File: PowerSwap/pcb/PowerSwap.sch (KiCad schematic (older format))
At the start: 11 parts

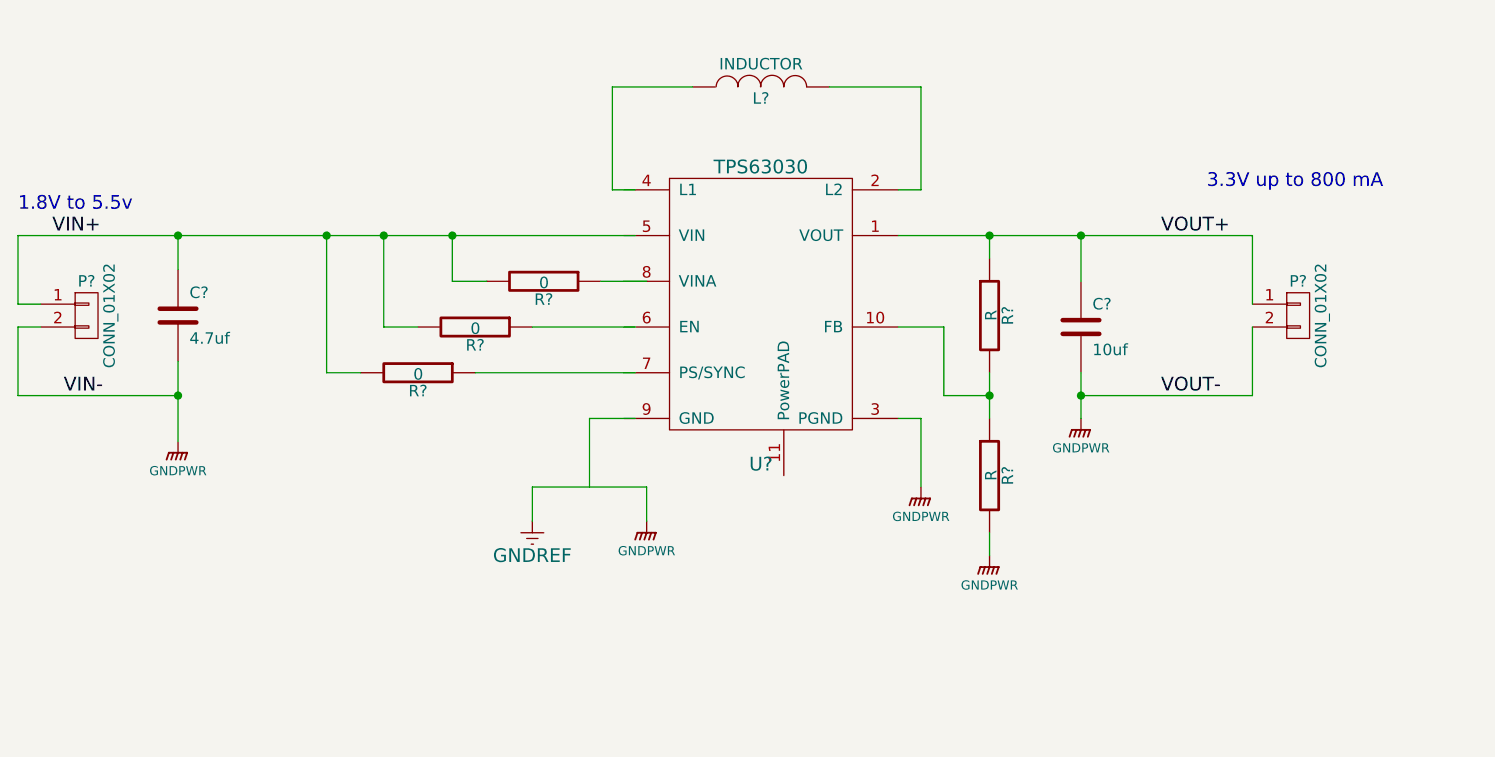
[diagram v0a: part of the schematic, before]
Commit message: PS updated schematic with testpoints and option a/b applications
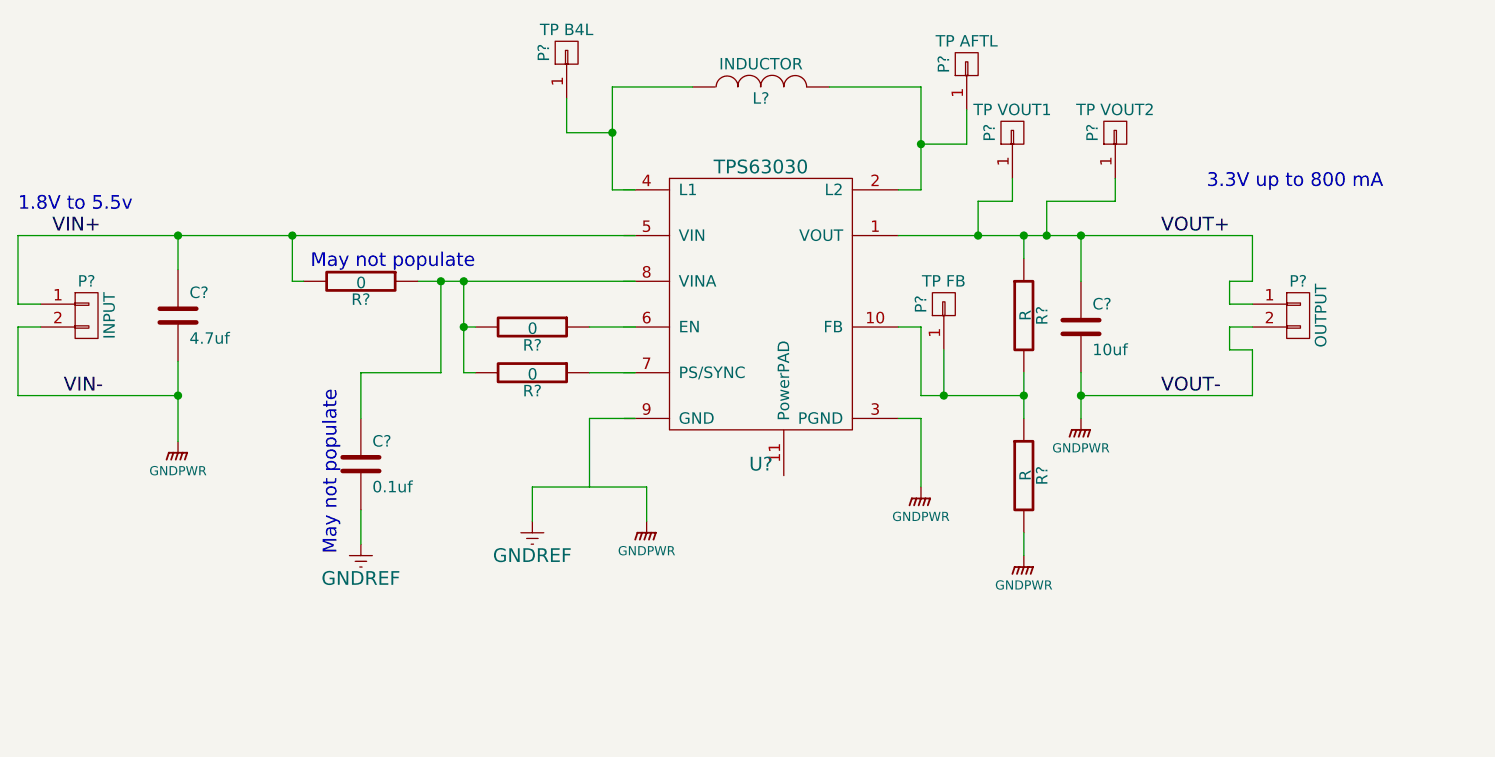
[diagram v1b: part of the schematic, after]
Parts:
- removed R? (x3): 0, symbol R
- added C?: 0.1uf, symbol C
- added P?: TP FB, symbol CONN_01X01
- added P?: TP B4L, symbol CONN_01X01
- added P?: TP AFTL, symbol CONN_01X01
- added P?: TP VOUT1, symbol CONN_01X01
- added P?: TP VOUT2, symbol CONN_01X01
- added R? (x3): 0, symbol R
- P?: value CONN_01X02 -> OUTPUT
- P?: value CONN_01X02 -> INPUT
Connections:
- wire segments 42 -> 62
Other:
- note added: "May not populate"
- moved on the sheet: R?

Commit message: PS updated schematic with testpoints and option a/b applications
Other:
- note removed: "3.3V up to 800 mA"
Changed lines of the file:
@@
 Wire Wire Line
 	4750 2850 6300 2850
-Text Notes 6100 2650 0    60   ~ 0
-3.3V up to 800 mA
 Wire Wire Line
 	5550 2850 5550 3050

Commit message: PS updated schematic with testpoints and option a/b applications
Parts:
- C?: value 4.7uf -> 4.7/10uf
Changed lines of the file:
@@
 P 1600 3200
 F 0 "C?" H 1650 3300 50  0000 L CNN
-F 1 "4.7uf" H 1650 3100 50  0000 L CNN
+F 1 "4.7/10uf" H 1650 3100 50  0000 L CNN
 F 2 "" H 1638 3050 30  0000 C CNN
 F 3 "" H 1600 3200 60  0000 C CNN

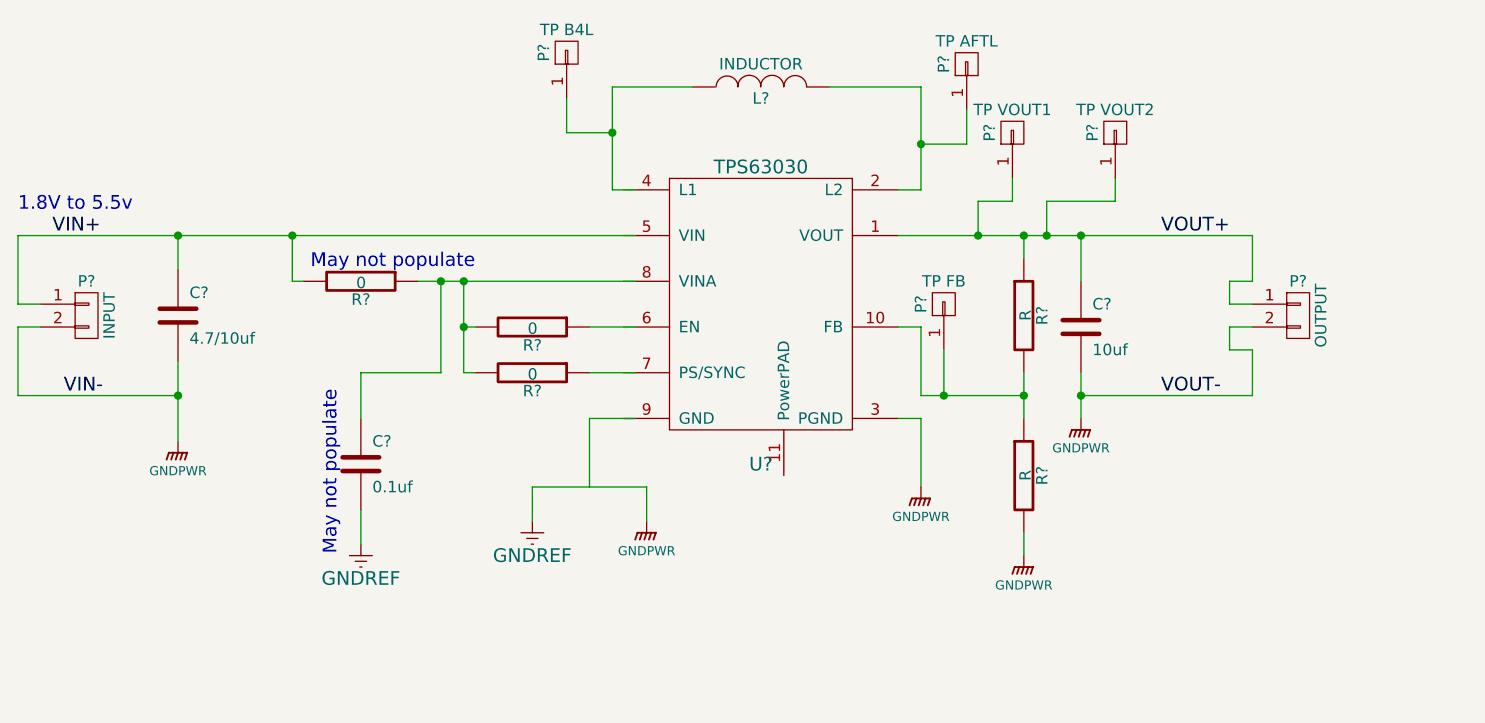
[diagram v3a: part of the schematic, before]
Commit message: PS added PowerPAD to tps6030, created footprint for tps6030
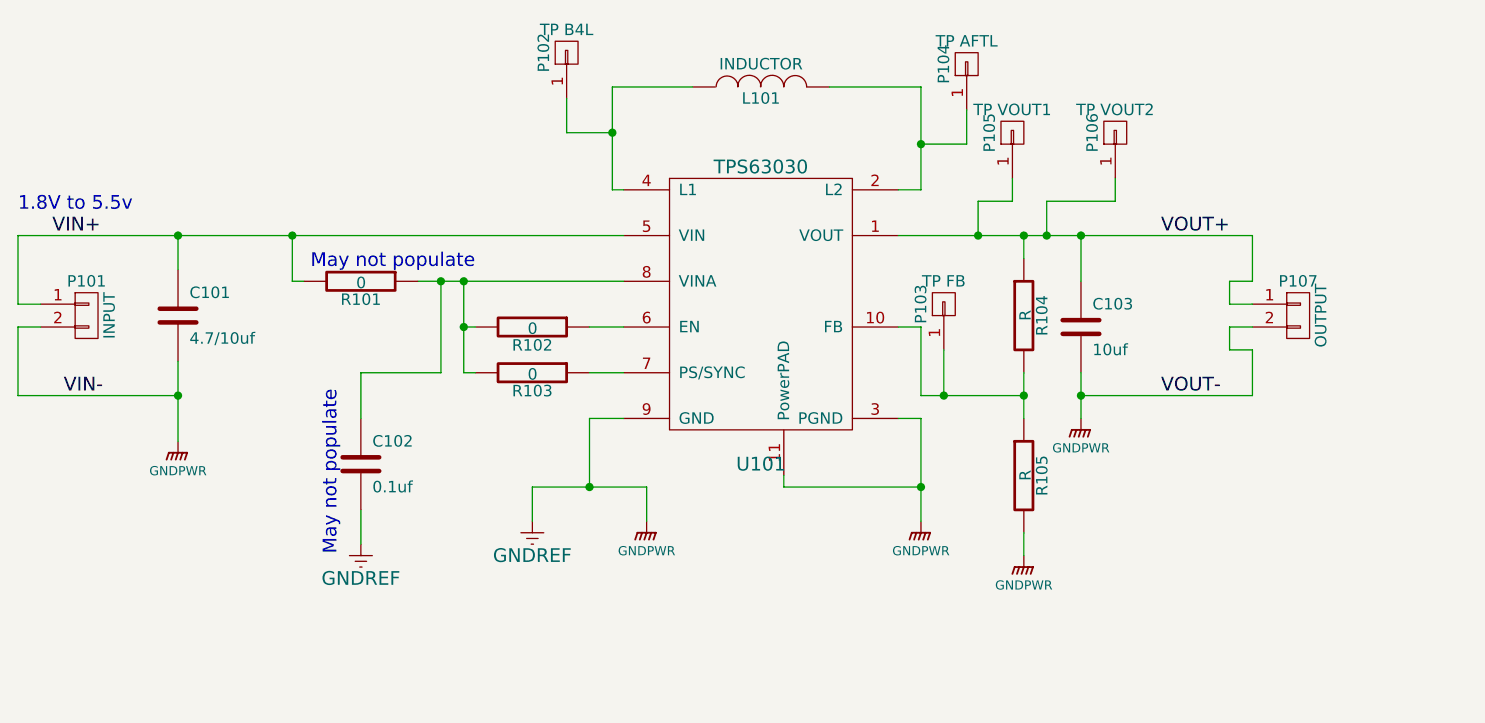
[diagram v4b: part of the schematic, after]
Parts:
- gave numbers to parts that had none: 17
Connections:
- wire segments 62 -> 64
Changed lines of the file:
@@
 v1
 $Comp
-L TPS63030 U?
+L TPS63030 U101
 U 1 1 55BC574B
 P 4150 3150
-F 0 "U?" H 4150 2450 60  0000 C CNN
+F 0 "U101" H 4150 2450 60  0000 C CNN
 F 1 "TPS63030" H 4150 3750 60  0000 C CNN
 F 2 "" H 4150 3150 60  0000 C CNN
@@
 $EndComp
 $Comp
-L INDUCTOR L?
+L INDUCTOR L101
 U 1 1 55BC57E7
 P 4150 2200
-F 0 "L?" V 4100 2200 50  0000 C CNN
+F 0 "L101" V 4100 2200 50  0000 C CNN
 F 1 "INDUCTOR" V 4250 2200 50  0000 C CNN
 F 2 "" H 4150 2200 60  0000 C CNN
@@
 $EndComp
 Wire Wire Line
-	3500 2650 3600 2650
-Wire Wire Line
-	3500 2200 3500 2650
-Wire Wire Line
 	3500 2200 3850 2200
 Wire Wire Line
@@
 Wire Wire Line
 	4850 2200 4450 2200
-Wire Wire Line
-	900  2850 3600 2850
 Text Notes 900  2750 0    60   ~ 0
 1.8V to 5.5v
@@
 Connection ~ 1600 2850
 $Comp
-L C C?
+L C C101
 U 1 1 55BC58C4
 P 1600 3200
-F 0 "C?" H 1650 3300 50  0000 L CNN
+F 0 "C101" H 1650 3300 50  0000 L CNN
 F 1 "4.7/10uf" H 1650 3100 50  0000 L CNN
 F 2 "" H 1638 3050 30  0000 C CNN
@@
 Connection ~ 1600 3550
 $Comp
-L GNDPWR #PWR?
+L GNDPWR #PWR01
 U 1 1 55BC592A
 P 1600 3750
-F 0 "#PWR?" H 1600 3550 40  0001 C CNN
+F 0 "#PWR01" H 1600 3550 40  0001 C CNN
 F 1 "GNDPWR" H 1600 3620 40  0000 C CNN
 F 2 "" H 1600 3700 60  0000 C CNN
@@
 $EndComp
 Wire Wire Line
-	3600 3650 3400 3650
-Wire Wire Line
-	3400 3650 3400 3950
-Wire Wire Line
 	3150 3950 3650 3950
 Wire Wire Line
@@
 	3650 3950 3650 4100
 $Comp
-L GNDPWR #PWR?
+L GNDPWR #PWR02
 U 1 1 55BC59FC
 P 3650 4100
-F 0 "#PWR?" H 3650 3900 40  0001 C CNN
+F 0 "#PWR02" H 3650 3900 40  0001 C CNN
 F 1 "GNDPWR" H 3650 3970 40  0000 C CNN
 F 2 "" H 3650 4050 60  0000 C CNN
@@
 	4750 3650 4850 3650
 Wire Wire Line
-	4850 3650 4850 3950
-$Comp
-L GNDPWR #PWR?
+	4850 3650 4850 4100
+$Comp
+L GNDPWR #PWR03
 U 1 1 55BC5A5E
-P 4850 3950
-F 0 "#PWR?" H 4850 3750 40  0001 C CNN
-F 1 "GNDPWR" H 4850 3820 40  0000 C CNN
-F 2 "" H 4850 3900 60  0000 C CNN
-F 3 "" H 4850 3900 60  0000 C CNN
-	1    4850 3950
+P 4850 4100
+F 0 "#PWR03" H 4850 3900 40  0001 C CNN
+F 1 "GNDPWR" H 4850 3970 40  0000 C CNN
+F 2 "" H 4850 4050 60  0000 C CNN
+F 3 "" H 4850 4050 60  0000 C CNN
+	1    4850 4100
 	1    0    0    -1
 $EndComp
@@
 Connection ~ 5550 2850
 $Comp
-L C C?
+L C C103
 U 1 1 55BC5BAF
 P 5550 3250
-F 0 "C?" H 5600 3350 50  0000 L CNN
+F 0 "C103" H 5600 3350 50  0000 L CNN
 F 1 "10uf" H 5600 3150 50  0000 L CNN
 F 2 "" H 5588 3100 30  0000 C CNN
@@
 Connection ~ 5550 3550
 $Comp
-L GNDPWR #PWR?
+L GNDPWR #PWR04
 U 1 1 55BC5C83
 P 5550 3650
-F 0 "#PWR?" H 5550 3450 40  0001 C CNN
+F 0 "#PWR04" H 5550 3450 40  0001 C CNN
 F 1 "GNDPWR" H 5550 3520 40  0000 C CNN
 F 2 "" H 5550 3600 60  0000 C CNN
@@
 $EndComp
 $Comp
-L CONN_01X02 P?
+L CONN_01X02 P107
 U 1 1 55BC5CD5
 P 6500 3200
-F 0 "P?" H 6500 3350 50  0000 C CNN
+F 0 "P107" H 6500 3350 50  0000 C CNN
 F 1 "OUTPUT" V 6600 3200 50  0000 C CNN
 F 2 "" H 6500 3200 60  0000 C CNN
@@
 VOUT-
 $Comp
-L CONN_01X02 P?
+L CONN_01X02 P101
 U 1 1 55BC5DDE
 P 1200 3200
-F 0 "P?" H 1200 3350 50  0000 C CNN
+F 0 "P101" H 1200 3350 50  0000 C CNN
 F 1 "INPUT" V 1300 3200 50  0000 C CNN
 F 2 "" H 1200 3200 60  0000 C CNN
@@
 VIN-
 $Comp
-L GNDREF #PWR?
+L GNDREF #PWR05
 U 1 1 55BC61AA
 P 3150 4100
-F 0 "#PWR?" H 3150 3850 60  0001 C CNN
+F 0 "#PWR05" H 3150 3850 60  0001 C CNN
 F 1 "GNDREF" H 3150 3950 60  0000 C CNN
 F 2 "" H 3150 4100 60  0000 C CNN
@@
 $EndComp
 $Comp
-L R R?
+L R R104
 U 1 1 55BC6276
 P 5300 3200
-F 0 "R?" V 5380 3200 50  0000 C CNN
+F 0 "R104" V 5380 3200 50  0000 C CNN
 F 1 "R" V 5307 3201 50  0000 C CNN
 F 2 "" V 5230 3200 30  0000 C CNN
@@
 $EndComp
 $Comp
-L R R?
+L R R105
 U 1 1 55BC62A0
 P 5300 3900
-F 0 "R?" V 5380 3900 50  0000 C CNN
+F 0 "R105" V 5380 3900 50  0000 C CNN
 F 1 "R" V 5307 3901 50  0000 C CNN
 F 2 "" V 5230 3900 30  0000 C CNN
@@
 	4850 3550 5300 3550
 $Comp
-L GNDPWR #PWR?
+L GNDPWR #PWR06
 U 1 1 55BC637F
 P 5300 4250
-F 0 "#PWR?" H 5300 4050 40  0001 C CNN
+F 0 "#PWR06" H 5300 4050 40  0001 C CNN
 F 1 "GNDPWR" H 5300 4120 40  0000 C CNN
 F 2 "" H 5300 4200 60  0000 C CNN
@@
 	5300 4150 5300 4250
 $Comp
-L CONN_01X01 P?
+L CONN_01X01 P103
 U 1 1 55BC6DD8
 P 4950 3150
-F 0 "P?" H 4950 3250 50  0000 C CNN
+F 0 "P103" H 4950 3250 50  0000 C CNN
 F 1 "TP FB" V 5050 3150 50  0000 C CNN
 F 2 "" H 4950 3150 60  0000 C CNN
@@
 Connection ~ 4950 3550
 $Comp
-L CONN_01X01 P?
+L CONN_01X01 P102
 U 1 1 55BC7112
 P 3300 2050
-F 0 "P?" H 3300 2150 50  0000 C CNN
+F 0 "P102" H 3300 2150 50  0000 C CNN
 F 1 "TP B4L" V 3400 2050 50  0000 C CNN
 F 2 "" H 3300 2050 60  0000 C CNN
@@
 $EndComp
 $Comp
-L CONN_01X01 P?
+L CONN_01X01 P104
 U 1 1 55BC7173
 P 5050 2100
-F 0 "P?" H 5050 2200 50  0000 C CNN
+F 0 "P104" H 5050 2200 50  0000 C CNN
 F 1 "TP AFTL" V 5150 2100 50  0000 C CNN
 F 2 "" H 5050 2100 60  0000 C CNN
@@
 Connection ~ 4850 2450
 $Comp
-L CONN_01X01 P?
+L CONN_01X01 P105
 U 1 1 55BC732C
 P 5250 2400
-F 0 "P?" H 5250 2500 50  0000 C CNN
+F 0 "P105" H 5250 2500 50  0000 C CNN
 F 1 "TP VOUT1" V 5350 2400 50  0000 C CNN
 F 2 "" H 5250 2400 60  0000 C CNN
@@
 	6200 3250 6300 3250
 $Comp
-L CONN_01X01 P?
+L CONN_01X01 P106
 U 1 1 55BC795D
 P 5700 2400
-F 0 "P?" H 5700 2500 50  0000 C CNN
+F 0 "P106" H 5700 2500 50  0000 C CNN
 F 1 "TP VOUT2" V 5800 2400 50  0000 C CNN
 F 2 "" H 5700 2400 60  0000 C CNN
@@
 	5700 2700 5700 2600
 Connection ~ 5400 2850
-Wire Wire Line
-	2650 3050 3600 3050
-$Comp
-L R R?
+$Comp
+L R R101
 U 1 1 55BC7CA3
 P 2400 3050
-F 0 "R?" V 2480 3050 50  0000 C CNN
+F 0 "R101" V 2480 3050 50  0000 C CNN
 F 1 "0" V 2407 3051 50  0000 C CNN
 F 2 "" V 2330 3050 30  0000 C CNN
@@
 Connection ~ 2100 2850
 $Comp
-L R R?
+L R R102
 U 1 1 55BC7EEF
 P 3150 3250
-F 0 "R?" V 3230 3250 50  0000 C CNN
+F 0 "R102" V 3230 3250 50  0000 C CNN
 F 1 "0" V 3157 3251 50  0000 C CNN
 F 2 "" V 3080 3250 30  0000 C CNN
@@
 $EndComp
 Wire Wire Line
-	3600 3250 3400 3250
-Wire Wire Line
 	2900 3250 2850 3250
 Wire Wire Line
@@
 Connection ~ 2850 3050
 $Comp
-L R R?
+L R R103
 U 1 1 55BC80A9
 P 3150 3450
-F 0 "R?" V 3230 3450 50  0000 C CNN
+F 0 "R103" V 3230 3450 50  0000 C CNN
 F 1 "0" V 3157 3451 50  0000 C CNN
 F 2 "" V 3080 3450 30  0000 C CNN
@@
 $EndComp
 Wire Wire Line
-	3600 3450 3400 3450
-Wire Wire Line
 	2400 3450 2750 3450
 Wire Wire Line
@@
 	2400 3450 2400 3650
 $Comp
-L C C?
+L C C102
 U 1 1 55BC84DC
 P 2400 3850
-F 0 "C?" H 2450 3950 50  0000 L CNN
+F 0 "C102" H 2450 3950 50  0000 L CNN
 F 1 "0.1uf" H 2450 3750 50  0000 L CNN
 F 2 "" H 2438 3700 30  0000 C CNN
@@
 	2400 4050 2400 4200
 $Comp
-L GNDREF #PWR?
+L GNDREF #PWR07
 U 1 1 55BC85DF
 P 2400 4200
-F 0 "#PWR?" H 2400 3950 60  0001 C CNN
+F 0 "#PWR07" H 2400 3950 60  0001 C CNN
 F 1 "GNDREF" H 2400 4050 60  0000 C CNN
 F 2 "" H 2400 4200 60  0000 C CNN
@@
 Text Notes 2900 3000 2    60   ~ 0
 May not populate
+Wire Wire Line
+	3400 3450 3550 3450
+Wire Wire Line
+	3400 3250 3550 3250
+Wire Wire Line
+	900  2850 3550 2850
+Wire Wire Line
+	3500 2650 3550 2650
+Wire Wire Line
+	3500 2200 3500 2650
+Wire Wire Line
+	4250 3900 4250 3950
+Wire Wire Line
+	4250 3950 4850 3950
+Connection ~ 4850 3950
+Wire Wire Line
+	2650 3050 3550 3050
+Wire Wire Line
+	3550 3650 3400 3650
+Wire Wire Line
+	3400 3650 3400 3950
+Connection ~ 3400 3950
 $EndSCHEMATC
